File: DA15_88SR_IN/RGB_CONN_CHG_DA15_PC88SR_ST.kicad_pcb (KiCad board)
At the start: 2 copper layers, 24 x 16 mm, 3 parts, among them J1 98VM, J2 RGB, J3 HV

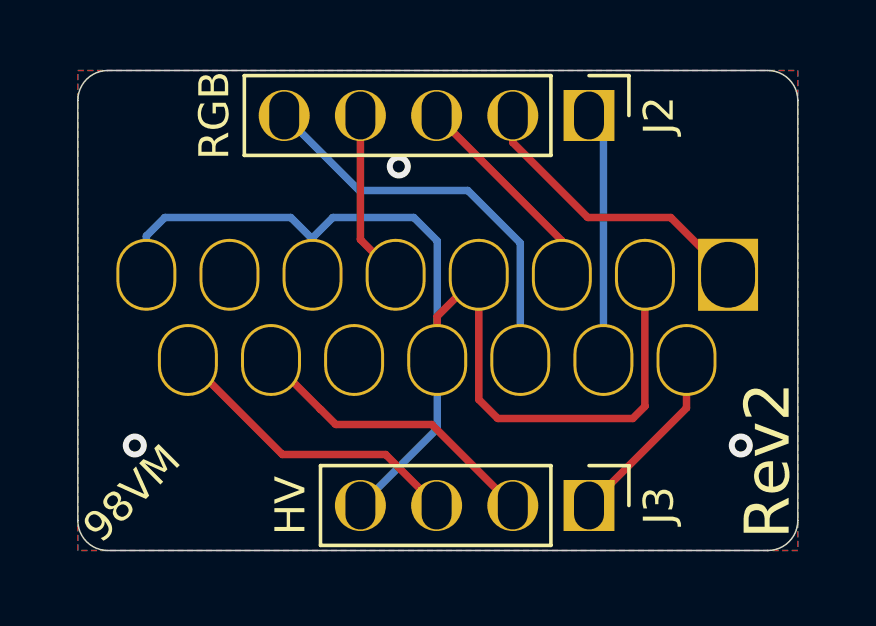
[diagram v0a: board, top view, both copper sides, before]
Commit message: update f_silk
added "Licensed under CERN-OHL-W v2"
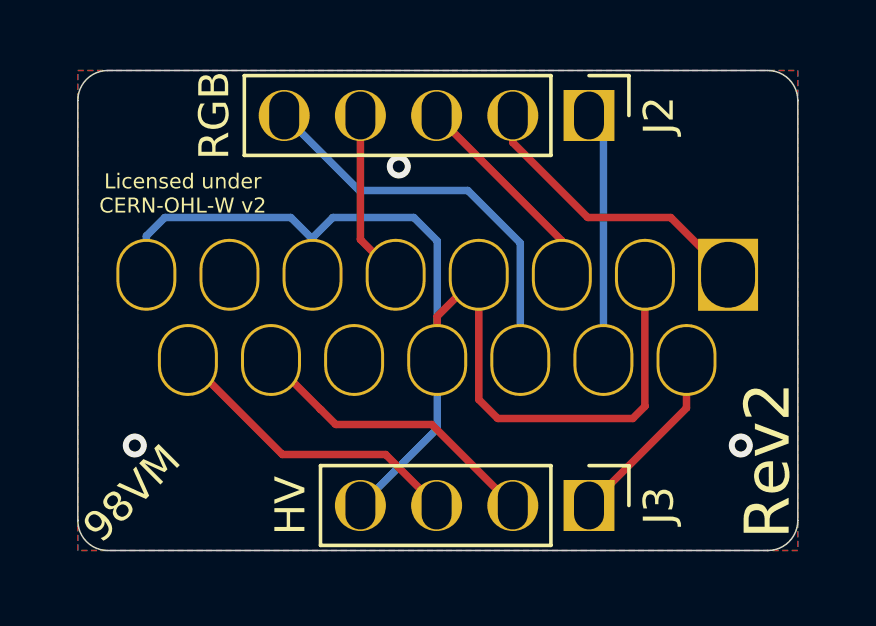
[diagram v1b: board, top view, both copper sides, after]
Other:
- board text added: "Licensed under CERN-OHL-W v2"
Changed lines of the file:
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@@
   (general
     (thickness 1.6)
-    (drawings 11)
+    (drawings 12)
     (tracks 46)
     (zones 0)
@@
       (effects (font (size 1 1) (thickness 0.15)))
     )
+    (fp_line (start 1.8 -1.8) (end -1.8 -1.8) (layer F.CrtYd) (width 0.05))
+    (fp_line (start 1.8 9.4) (end 1.8 -1.8) (layer F.CrtYd) (width 0.05))
+    (fp_line (start -1.8 9.4) (end 1.8 9.4) (layer F.CrtYd) (width 0.05))
+    (fp_line (start -1.8 -1.8) (end -1.8 9.4) (layer F.CrtYd) (width 0.05))
+    (fp_line (start -1.33 -1.33) (end 0 -1.33) (layer F.SilkS) (width 0.12))
+    (fp_line (start -1.33 0) (end -1.33 -1.33) (layer F.SilkS) (width 0.12))
+    (fp_line (start -1.33 1.27) (end 1.33 1.27) (layer F.SilkS) (width 0.12))
+    (fp_line (start 1.33 1.27) (end 1.33 8.95) (layer F.SilkS) (width 0.12))
+    (fp_line (start -1.33 1.27) (end -1.33 8.95) (layer F.SilkS) (width 0.12))
+    (fp_line (start -1.33 8.95) (end 1.33 8.95) (layer F.SilkS) (width 0.12))
+    (fp_line (start -1.27 -0.635) (end -0.635 -1.27) (layer F.Fab) (width 0.1))
+    (fp_line (start -1.27 8.89) (end -1.27 -0.635) (layer F.Fab) (width 0.1))
+    (fp_line (start 1.27 8.89) (end -1.27 8.89) (layer F.Fab) (width 0.1))
+    (fp_line (start 1.27 -1.27) (end 1.27 8.89) (layer F.Fab) (width 0.1))
     (fp_line (start -0.635 -1.27) (end 1.27 -1.27) (layer F.Fab) (width 0.1))
-    (fp_line (start 1.27 -1.27) (end 1.27 8.89) (layer F.Fab) (width 0.1))
-    (fp_line (start 1.27 8.89) (end -1.27 8.89) (layer F.Fab) (width 0.1))
-    (fp_line (start -1.27 8.89) (end -1.27 -0.635) (layer F.Fab) (width 0.1))
-    (fp_line (start -1.27 -0.635) (end -0.635 -1.27) (layer F.Fab) (width 0.1))
-    (fp_line (start -1.33 8.95) (end 1.33 8.95) (layer F.SilkS) (width 0.12))
-    (fp_line (start -1.33 1.27) (end -1.33 8.95) (layer F.SilkS) (width 0.12))
-    (fp_line (start 1.33 1.27) (end 1.33 8.95) (layer F.SilkS) (width 0.12))
-    (fp_line (start -1.33 1.27) (end 1.33 1.27) (layer F.SilkS) (width 0.12))
-    (fp_line (start -1.33 0) (end -1.33 -1.33) (layer F.SilkS) (width 0.12))
-    (fp_line (start -1.33 -1.33) (end 0 -1.33) (layer F.SilkS) (width 0.12))
-    (fp_line (start -1.8 -1.8) (end -1.8 9.4) (layer F.CrtYd) (width 0.05))
-    (fp_line (start -1.8 9.4) (end 1.8 9.4) (layer F.CrtYd) (width 0.05))
-    (fp_line (start 1.8 9.4) (end 1.8 -1.8) (layer F.CrtYd) (width 0.05))
-    (fp_line (start 1.8 -1.8) (end -1.8 -1.8) (layer F.CrtYd) (width 0.05))
     (fp_text user %R (at 0 3.81) (layer F.Fab)
       (effects (font (size 1 1) (thickness 0.15)))
@@
       (effects (font (size 1 1) (thickness 0.15)))
     )
+    (fp_line (start -0.635 -1.27) (end 1.27 -1.27) (layer F.Fab) (width 0.1))
+    (fp_line (start 1.27 -1.27) (end 1.27 11.43) (layer F.Fab) (width 0.1))
+    (fp_line (start 1.27 11.43) (end -1.27 11.43) (layer F.Fab) (width 0.1))
+    (fp_line (start -1.27 11.43) (end -1.27 -0.635) (layer F.Fab) (width 0.1))
+    (fp_line (start -1.27 -0.635) (end -0.635 -1.27) (layer F.Fab) (width 0.1))
+    (fp_line (start -1.33 11.49) (end 1.33 11.49) (layer F.SilkS) (width 0.12))
+    (fp_line (start -1.33 1.27) (end -1.33 11.49) (layer F.SilkS) (width 0.12))
+    (fp_line (start 1.33 1.27) (end 1.33 11.49) (layer F.SilkS) (width 0.12))
+    (fp_line (start -1.33 1.27) (end 1.33 1.27) (layer F.SilkS) (width 0.12))
+    (fp_line (start -1.33 0) (end -1.33 -1.33) (layer F.SilkS) (width 0.12))
+    (fp_line (start -1.33 -1.33) (end 0 -1.33) (layer F.SilkS) (width 0.12))
+    (fp_line (start -1.8 -1.8) (end -1.8 11.95) (layer F.CrtYd) (width 0.05))
+    (fp_line (start -1.8 11.95) (end 1.8 11.95) (layer F.CrtYd) (width 0.05))
+    (fp_line (start 1.8 11.95) (end 1.8 -1.8) (layer F.CrtYd) (width 0.05))
     (fp_line (start 1.8 -1.8) (end -1.8 -1.8) (layer F.CrtYd) (width 0.05))
-    (fp_line (start 1.8 11.95) (end 1.8 -1.8) (layer F.CrtYd) (width 0.05))
-    (fp_line (start -1.8 11.95) (end 1.8 11.95) (layer F.CrtYd) (width 0.05))
-    (fp_line (start -1.8 -1.8) (end -1.8 11.95) (layer F.CrtYd) (width 0.05))
-    (fp_line (start -1.33 -1.33) (end 0 -1.33) (layer F.SilkS) (width 0.12))
-    (fp_line (start -1.33 0) (end -1.33 -1.33) (layer F.SilkS) (width 0.12))
-    (fp_line (start -1.33 1.27) (end 1.33 1.27) (layer F.SilkS) (width 0.12))
-    (fp_line (start 1.33 1.27) (end 1.33 11.49) (layer F.SilkS) (width 0.12))
-    (fp_line (start -1.33 1.27) (end -1.33 11.49) (layer F.SilkS) (width 0.12))
-    (fp_line (start -1.33 11.49) (end 1.33 11.49) (layer F.SilkS) (width 0.12))
-    (fp_line (start -1.27 -0.635) (end -0.635 -1.27) (layer F.Fab) (width 0.1))
-    (fp_line (start -1.27 11.43) (end -1.27 -0.635) (layer F.Fab) (width 0.1))
-    (fp_line (start 1.27 11.43) (end -1.27 11.43) (layer F.Fab) (width 0.1))
-    (fp_line (start 1.27 -1.27) (end 1.27 11.43) (layer F.Fab) (width 0.1))
-    (fp_line (start -0.635 -1.27) (end 1.27 -1.27) (layer F.Fab) (width 0.1))
     (fp_text user %R (at 0 5.08) (layer F.Fab)
       (effects (font (size 1 1) (thickness 0.15)))
@@
       (effects (font (size 1 1) (thickness 0.15)))
     )
+    (fp_line (start 29.8 5.35) (end -10.45 5.35) (layer B.CrtYd) (width 0.05))
+    (fp_line (start 29.8 -8.2) (end 29.8 5.35) (layer B.CrtYd) (width 0.05))
+    (fp_line (start -10.45 -8.2) (end 29.8 -8.2) (layer B.CrtYd) (width 0.05))
+    (fp_line (start -10.45 5.35) (end -10.45 -8.2) (layer B.CrtYd) (width 0.05))
+    (fp_line (start -2.32147 0.841744) (end -1.422202 -4.258256) (layer B.SilkS) (width 0.12))
+    (fp_line (start 21.71147 0.841744) (end 20.812202 -4.258256) (layer B.SilkS) (width 0.12))
+    (fp_line (start 0.212579 -5.63) (end 19.177421 -5.63) (layer B.SilkS) (width 0.12))
+    (fp_line (start -0.686689 2.79) (end 20.076689 2.79) (layer B.SilkS) (width 0.12))
+    (fp_line (start -2.273887 0.852163) (end -1.374619 -4.247837) (layer B.Fab) (width 0.1))
+    (fp_line (start 21.663887 0.852163) (end 20.764619 -4.247837) (layer B.Fab) (width 0.1))
+    (fp_line (start 0.201073 -5.57) (end 19.188927 -5.57) (layer B.Fab) (width 0.1))
+    (fp_line (start -0.698194 2.73) (end 20.088194 2.73) (layer B.Fab) (width 0.1))
+    (fp_line (start 0 5.351325) (end -0.25 5.784338) (layer B.SilkS) (width 0.12))
+    (fp_line (start 0.25 5.784338) (end 0 5.351325) (layer B.SilkS) (width 0.12))
+    (fp_line (start -0.25 5.784338) (end 0.25 5.784338) (layer B.SilkS) (width 0.12))
+    (fp_line (start -9.965 -6.67) (end -9.965 3.83) (layer B.SilkS) (width 0.12))
+    (fp_line (start 28.295 -7.73) (end -8.905 -7.73) (layer B.SilkS) (width 0.12))
+    (fp_line (start 29.355 3.83) (end 29.355 -6.67) (layer B.SilkS) (width 0.12))
+    (fp_line (start -8.905 4.89) (end 28.295 4.89) (layer B.SilkS) (width 0.12))
+    (fp_line (start -9.905 -6.67) (end -9.905 3.83) (layer B.Fab) (width 0.1))
+    (fp_line (start 28.295 -7.67) (end -8.905 -7.67) (layer B.Fab) (width 0.1))
+    (fp_line (start 29.295 3.83) (end 29.295 -6.67) (layer B.Fab) (width 0.1))
     (fp_line (start -8.905 4.83) (end 28.295 4.83) (layer B.Fab) (width 0.1))
-    (fp_line (start 29.295 3.83) (end 29.295 -6.67) (layer B.Fab) (width 0.1))
-    (fp_line (start 28.295 -7.67) (end -8.905 -7.67) (layer B.Fab) (width 0.1))
-    (fp_line (start -9.905 -6.67) (end -9.905 3.83) (layer B.Fab) (width 0.1))
-    (fp_line (start -8.905 4.89) (end 28.295 4.89) (layer B.SilkS) (width 0.12))
-    (fp_line (start 29.355 3.83) (end 29.355 -6.67) (layer B.SilkS) (width 0.12))
-    (fp_line (start 28.295 -7.73) (end -8.905 -7.73) (layer B.SilkS) (width 0.12))
-    (fp_line (start -9.965 -6.67) (end -9.965 3.83) (layer B.SilkS) (width 0.12))
-    (fp_line (start -0.25 5.784338) (end 0.25 5.784338) (layer B.SilkS) (width 0.12))
-    (fp_line (start 0.25 5.784338) (end 0 5.351325) (layer B.SilkS) (width 0.12))
-    (fp_line (start 0 5.351325) (end -0.25 5.784338) (layer B.SilkS) (width 0.12))
-    (fp_line (start -0.698194 2.73) (end 20.088194 2.73) (layer B.Fab) (width 0.1))
-    (fp_line (start 0.201073 -5.57) (end 19.188927 -5.57) (layer B.Fab) (width 0.1))
-    (fp_line (start 21.663887 0.852163) (end 20.764619 -4.247837) (layer B.Fab) (width 0.1))
-    (fp_line (start -2.273887 0.852163) (end -1.374619 -4.247837) (layer B.Fab) (width 0.1))
-    (fp_line (start -0.686689 2.79) (end 20.076689 2.79) (layer B.SilkS) (width 0.12))
-    (fp_line (start 0.212579 -5.63) (end 19.177421 -5.63) (layer B.SilkS) (width 0.12))
-    (fp_line (start 21.71147 0.841744) (end 20.812202 -4.258256) (layer B.SilkS) (width 0.12))
-    (fp_line (start -2.32147 0.841744) (end -1.422202 -4.258256) (layer B.SilkS) (width 0.12))
-    (fp_line (start -10.45 5.35) (end -10.45 -8.2) (layer B.CrtYd) (width 0.05))
-    (fp_line (start -10.45 -8.2) (end 29.8 -8.2) (layer B.CrtYd) (width 0.05))
-    (fp_line (start 29.8 -8.2) (end 29.8 5.35) (layer B.CrtYd) (width 0.05))
-    (fp_line (start 29.8 5.35) (end -10.45 5.35) (layer B.CrtYd) (width 0.05))
     (fp_text user %R (at 9.695 -1.42) (layer B.Fab)
       (effects (font (size 1 1) (thickness 0.15)) (justify mirror))
@@
     )
   )
+  (gr_text "Licensed under\nCERN-OHL-W v2" (at 126.5 82.1) (layer F.SilkS)
+    (effects (font (size 0.5 0.5) (thickness 0.1)))
+  )
   (gr_text Rev2 (at 146 91 90) (layer F.SilkS)
